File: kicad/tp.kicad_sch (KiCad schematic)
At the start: 16 parts, among them J2 MAX30102_Header, SW1 SWITCH_MODE, SW2 ALARM_OFF, U1 HM10

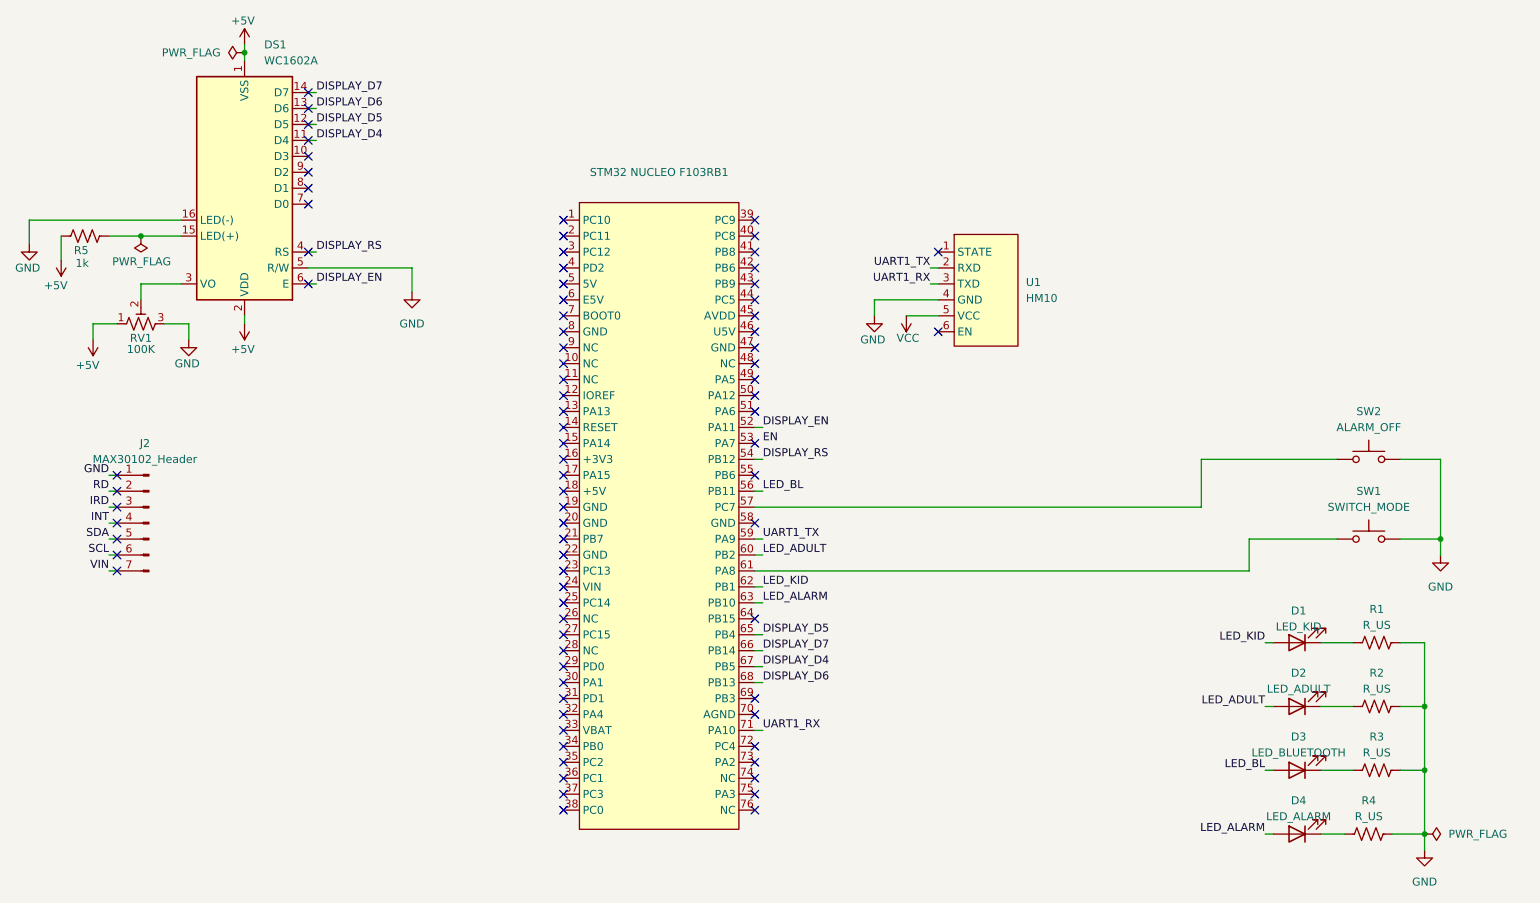
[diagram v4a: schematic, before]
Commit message: feat(sch): agrega symbols y conexiones faltantes
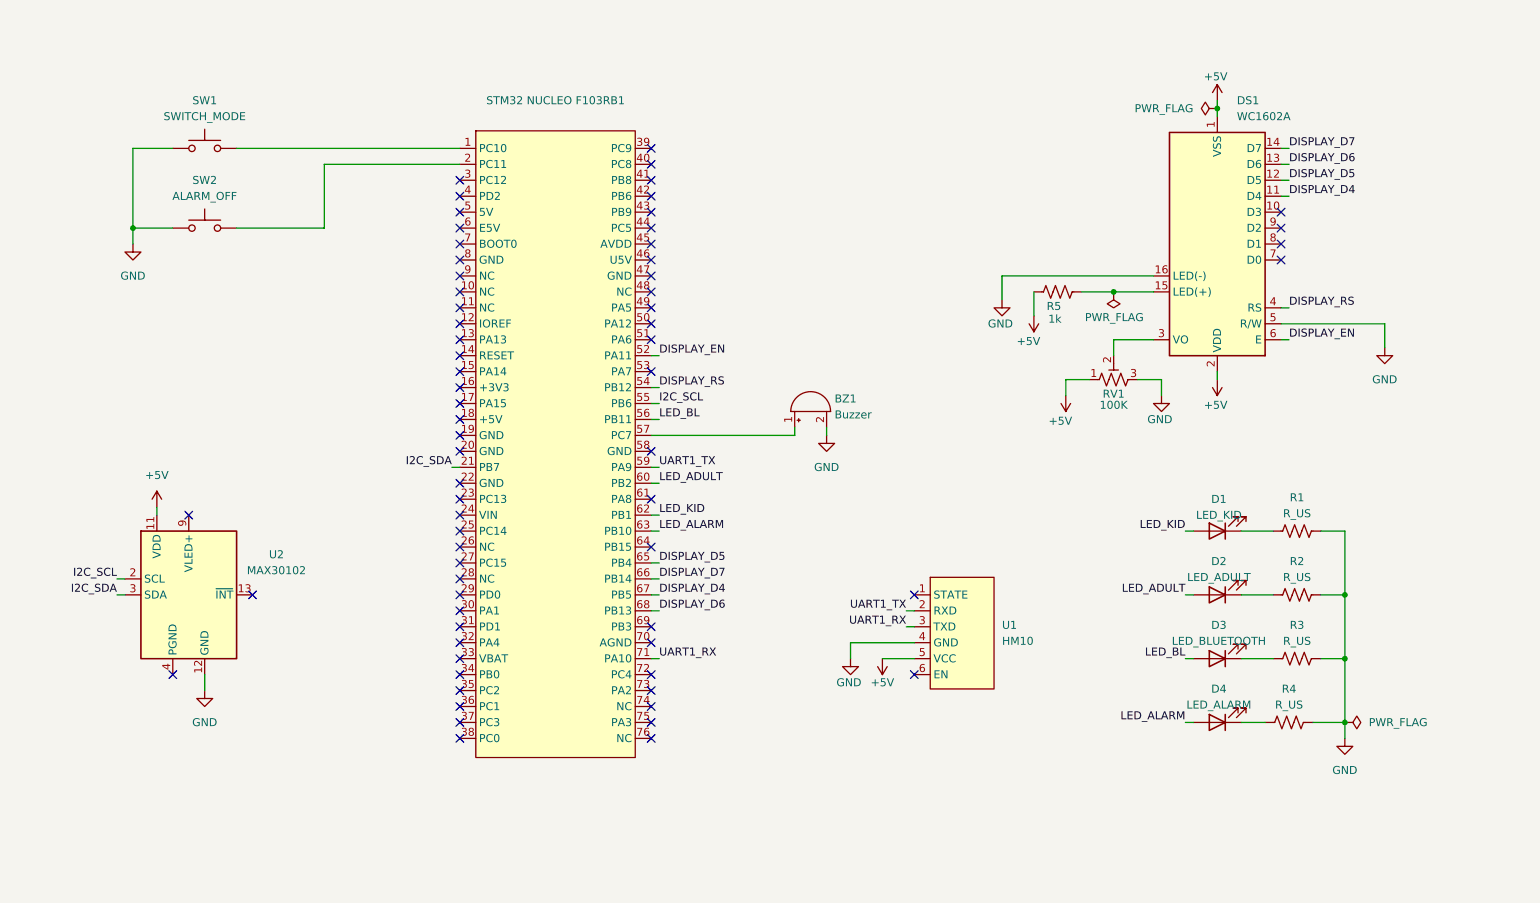
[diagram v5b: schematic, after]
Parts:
- removed J2: MAX30102_Header, symbol Connector:Conn_01x07_Pin
- added BZ1: Buzzer, symbol Device:Buzzer
- added U2: MAX30102, OptoDevice:Maxim_OLGA-14_3.3x5.6mm_P0.8mm, symbol Sensor:MAX30102
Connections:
- net VCC is gone; now on net +5V: U1.5 (VCC)
- net +5V: now also U2.11 (VDD)
- net GND: now also BZ1.2 (-), U2.12 (GND)
- net at SW1.2: now also STM32 NUCLEO F103RB1.1 (PC10); no longer STM32 NUCLEO F103RB1.61 (PA8)
- net at SW2.2: now also STM32 NUCLEO F103RB1.2 (PC11); no longer STM32 NUCLEO F103RB1.57 (PC7)
- net I2C_SDA: now reaches STM32 NUCLEO F103RB1.21 (PB7)
- net I2C_SDA: now also U2.3 (SDA)
- net I2C_SCL: now reaches STM32 NUCLEO F103RB1.55 (PB6)
- net I2C_SCL: now also U2.2 (SCL)
- new net: U2.10 (VLED+), U2.9 (VLED+)
- new net: BZ1.1 (+), STM32 NUCLEO F103RB1.57 (PC7)
- no-connect marks 81 -> 68
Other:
- moved on the sheet: D1, D2, D3, D4, DS1, R1, R2, R3, R4, R5, RV1, STM32 NUCLEO F103RB1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

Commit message: fix(sch): actualizo el simbolo de la nucleo
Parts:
- removed STM32 NUCLEO F103RB1: ~, symbol STM32_NUCLEO:NUCLEO-F103RB
- added U1: STM32 NUCLEO F103RB, STM32:NUCLEO F103RB, symbol STM32_NUCLEO:NUCLEO-F103RB
- renumbered U1 to U3
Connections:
- net DISPLAY_D4: now also U1.67 (PB5)
- net DISPLAY_D5: now also U1.65 (PB4)
- net DISPLAY_D6: now also U1.68 (PB13)
- net DISPLAY_D7: now also U1.66 (PB14)
- net DISPLAY_EN: now also U1.52 (PA11)
- net DISPLAY_RS: now also U1.54 (PB12)
- net I2C_SCL: now also U1.55 (PB6)
- net I2C_SDA: now also U1.21 (PB7)
- net LED_ADULT: now also U1.60 (PB2)
- net LED_ALARM: now also U1.63 (PB10)
- net LED_BL: now also U1.56 (PB11)
- net LED_KID: now also U1.62 (PB1)
- net UART1_RX: now also U1.71 (PA10)
- net UART1_TX: now also U1.59 (PA9)
- net at SW1.2: now also U1.1 (PC10)
- net at SW2.2: now also U1.2 (PC11)
- net at BZ1.1 (+): now also U1.57 (PC7)
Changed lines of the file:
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@@
 		(dnp no)
 		(fields_autoplaced yes)
-		(property "Reference" "U1"
+		(property "Reference" "U3"
 			(at 180.34 115.3159 0)
 			(effects
@@
 			(project ""
 				(path "/4321da81-5d44-4e9a-b537-a2876d1011a9"
-					(reference "U1")
+					(reference "U3")
 					(unit 1)
 				)
@@
 	)
 	(symbol
+		(lib_id "STM32_NUCLEO:NUCLEO-F103RB")
+		(at 109.22 85.09 0)
+		(unit 1)
+		(exclude_from_sim no)
+		(in_bom yes)
+		(on_board yes)
+		(dnp no)
+		(fields_autoplaced yes)
+		(property "Reference" "U1"
+			(at 109.22 31.75 0)
+			(effects
+				(font
+					(size 1.27 1.27)
+				)
+			)
+		)
+		(property "Value" "STM32 NUCLEO F103RB"
+			(at 109.22 34.29 0)
+			(effects
+				(font
+					(size 1.27 1.27)
+				)
+			)
+		)
+		(property "Footprint" "STM32:NUCLEO F103RB"
+			(at 109.22 85.09 0)
+			(effects
+				(font
+					(size 1.27 1.27)
+				)
+				(hide yes)
+			)
+		)
+		(property "Datasheet" ""
+			(at 109.22 85.09 0)
+			(effects
+				(font
+					(size 1.27 1.27)
+				)
+				(hide yes)
+			)
+		)
+		(property "Description" ""
+			(at 109.22 85.09 0)
+			(effects
+				(font
+					(size 1.27 1.27)
+				)
+				(hide yes)
+			)
+		)
+		(pin "66"
+		)
+		(pin "47"
+		)
+		(pin "43"
+		)
+		(pin "2"
+		)
+		(pin "44"
+		)
+		(pin "19"
+		)
+		(pin "63"
+		)
+		(pin "74"
+		)
+		(pin "73"
+		)
+		(pin "51"
+		)
+		(pin "67"
+		)
+		(pin "64"
+		)
+		(pin "55"
+		)
+		(pin "24"
+		)
+		(pin "37"
+		)
+		(pin "33"
+		)
+		(pin "50"
+		)
+		(pin "53"
+		)
+		(pin "27"
+		)
+		(pin "30"
+		)
+		(pin "34"
+		)
+		(pin "22"
+		)
+		(pin "57"
+		)
+		(pin "48"
+		)
+		(pin "56"
+		)
+		(pin "70"
+		)
+		(pin "60"
+		)
+		(pin "32"
+		)
+		(pin "42"
+		)
+		(pin "61"
+		)
+		(pin "28"
+		)
+		(pin "31"
+		)
+		(pin "58"
+		)
+		(pin "52"
+		)
+		(pin "62"
+		)
+		(pin "71"
+		)
+		(pin "46"
+		)
+		(pin "26"
+		)
+		(pin "45"
+		)
+		(pin "29"
+		)
+		(pin "65"
+		)
+		(pin "41"
+		)
+		(pin "38"
+		)
+		(pin "18"
+		)
+		(pin "54"
+		)
+		(pin "21"
+		)
+		(pin "20"
+		)
+		(pin "16"
+		)
+		(pin "9"
+		)
+		(pin "8"
+		)
+		(pin "7"
+		)
+		(pin "6"
+		)
+		(pin "5"
+		)
+		(pin "4"
+		)
+		(pin "3"
+		)
+		(pin "1"
+		)
+		(pin "15"
+		)
+		(pin "14"
+		)
+		(pin "13"
+		)
+		(pin "12"
+		)
+		(pin "11"
+		)
+		(pin "10"
+		)
+		(pin "23"
+		)
+		(pin "72"
+		)
+		(pin "68"
+		)
+		(pin "75"
+		)
+		(pin "76"
+		)
+		(pin "17"
+		)
+		(pin "25"
+		)
+		(pin "59"
+		)
+		(pin "39"
+		)
+		(pin "69"
+		)
+		(pin "40"
+		)
+		(pin "36"
+		)
+		(pin "35"
+		)
+		(pin "49"
+		)
+		(instances
+			(project ""
+				(path "/4321da81-5d44-4e9a-b537-a2876d1011a9"
+					(reference "U1")
+					(unit 1)
+				)
+			)
+		)
+	)
+	(symbol
 		(lib_id "power:PWR_FLAG")
 		(at 234.95 130.81 270)
@@
 					(unit 1)
 				)
-			)
-		)
-	)
-	(symbol
-		(lib_id "STM32_NUCLEO:NUCLEO-F103RB")
-		(at 109.22 85.09 0)
-		(unit 1)
-		(exclude_from_sim no)
-		(in_bom yes)
-		(on_board yes)
-		(dnp no)
-		(fields_autoplaced yes)
-		(property "Reference" "STM32 NUCLEO F103RB1"
-			(at 109.22 31.75 0)
-			(effects
-				(font
-					(size 1.27 1.27)
-				)
-			)
-		)
-		(property "Value" "~"
-			(at 109.22 34.29 0)
-			(effects
-				(font
-					(size 1.27 1.27)
-				)
-			)
-		)
-		(property "Footprint" ""
-			(at 109.22 85.09 0)
-			(effects
-				(font
-					(size 1.27 1.27)
-				)
-				(hide yes)
-			)
-		)
-		(property "Datasheet" ""
-			(at 109.22 85.09 0)
-			(effects
-				(font
-					(size 1.27 1.27)
-				)
-				(hide yes)
-			)
-		)
-		(property "Description" ""
-			(at 109.22 85.09 0)
-			(effects
-				(font
-					(size 1.27 1.27)
-				)
-				(hide yes)
-			)
-		)
-		(pin "21"
-		)
-		(pin "75"
-		)
-		(pin "20"
-		)
-		(pin "63"
-		)
-		(pin "60"
-		)
-		(pin "61"
-		)
-		(pin "59"
-		)
-		(pin "58"
-		)
-		(pin "57"
-		)
-		(pin "70"
-		)
-		(pin "74"
-		)
-		(pin "72"
-		)
-		(pin "73"
-		)
-		(pin "71"
-		)
-		(pin "76"
-		)
-		(pin "2"
-		)
-		(pin "56"
-		)
-		(pin "23"
-		)
-		(pin "42"
-		)
-		(pin "44"
-		)
-		(pin "43"
-		)
-		(pin "32"
-		)
-		(pin "26"
-		)
-		(pin "50"
-		)
-		(pin "51"
-		)
-		(pin "52"
-		)
-		(pin "54"
-		)
-		(pin "53"
-		)
-		(pin "48"
-		)
-		(pin "49"
-		)
-		(pin "45"
-		)
-		(pin "35"
-		)
-		(pin "39"
-		)
-		(pin "33"
-		)
-		(pin "27"
-		)
-		(pin "28"
-		)
-		(pin "19"
-		)
-		(pin "25"
-		)
-		(pin "24"
-		)
-		(pin "65"
-		)
-		(pin "64"
-		)
-		(pin "29"
-		)
-		(pin "30"
-		)
-		(pin "22"
-		)
-		(pin "46"
-		)
-		(pin "47"
-		)
-		(pin "40"
-		)
-		(pin "41"
-		)
-		(pin "34"
-		)
-		(pin "62"
-		)
-		(pin "66"
-		)
-		(pin "31"
-		)
-		(pin "18"
-		)
-		(pin "69"
-		)
-		(pin "67"
-		)
-		(pin "68"
-		)
-		(pin "55"
-		)
-		(pin "36"
-		)
-		(pin "37"
-		)
-		(pin "17"
-		)
-		(pin "8"
-		)
-		(pin "7"
-		)
-		(pin "6"
-		)
-		(pin "5"
-		)
-		(pin "4"
-		)
-		(pin "3"
-		)
-		(pin "1"
-		)
-		(pin "38"
-		)
-		(pin "16"
-		)
-		(pin "15"
-		)
-		(pin "14"
-		)
-		(pin "13"
-		)
-		(pin "12"
-		)
-		(pin "11"
-		)
-		(pin "10"
-		)
-		(pin "9"
-		)
-		(instances
-			(project ""
-				(path "/4321da81-5d44-4e9a-b537-a2876d1011a9"
-					(reference "STM32 NUCLEO F103RB1")
-					(unit 1)
-				)

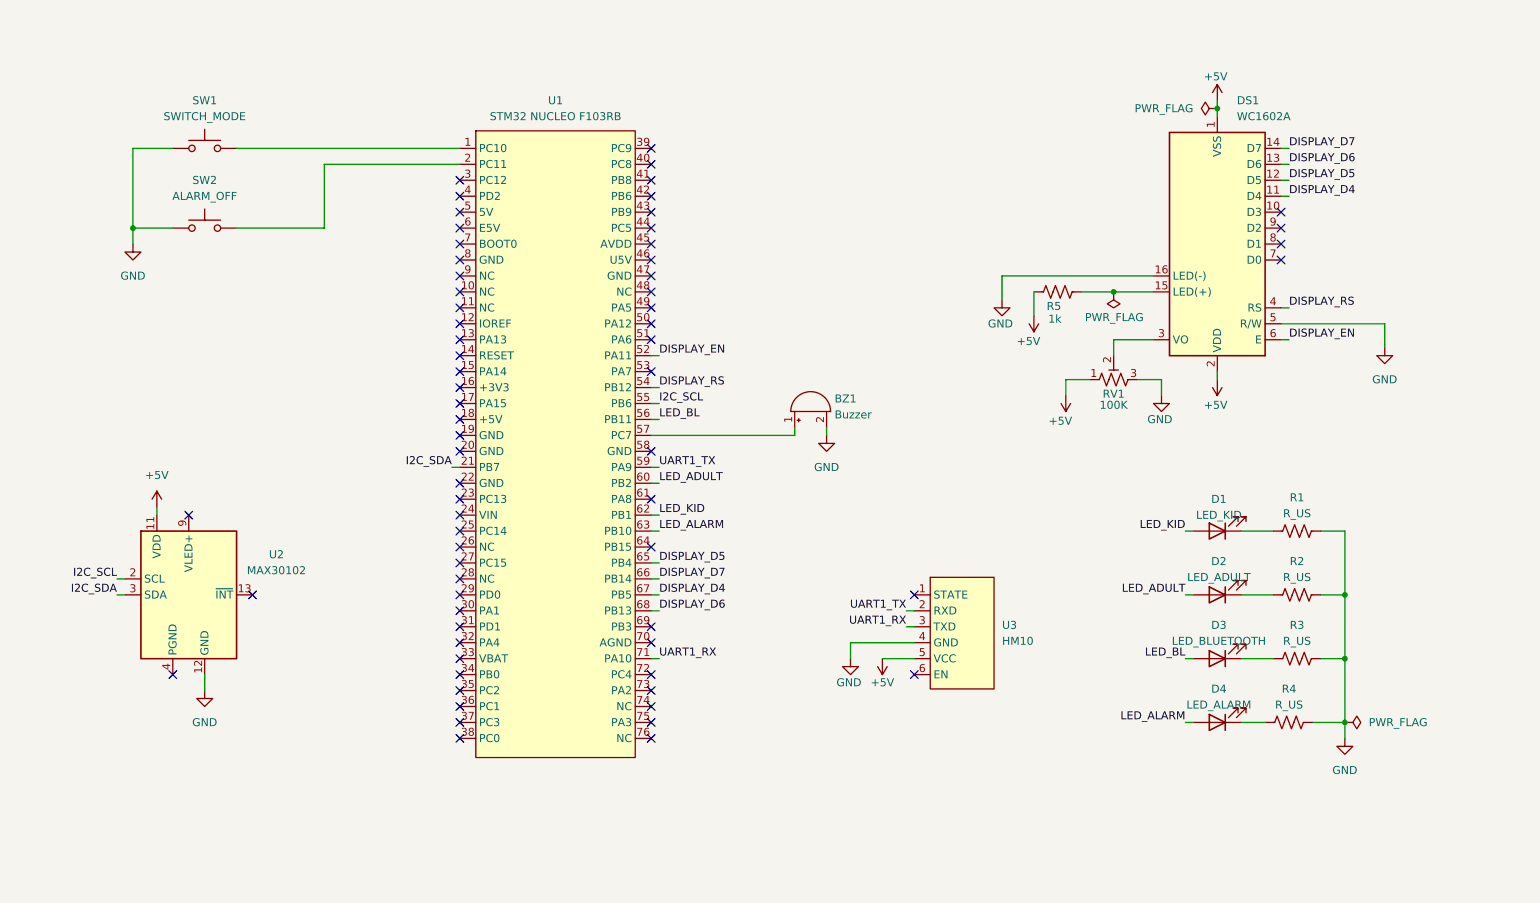
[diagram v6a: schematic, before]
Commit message: feat(sch): agrego las footprints de los componentes
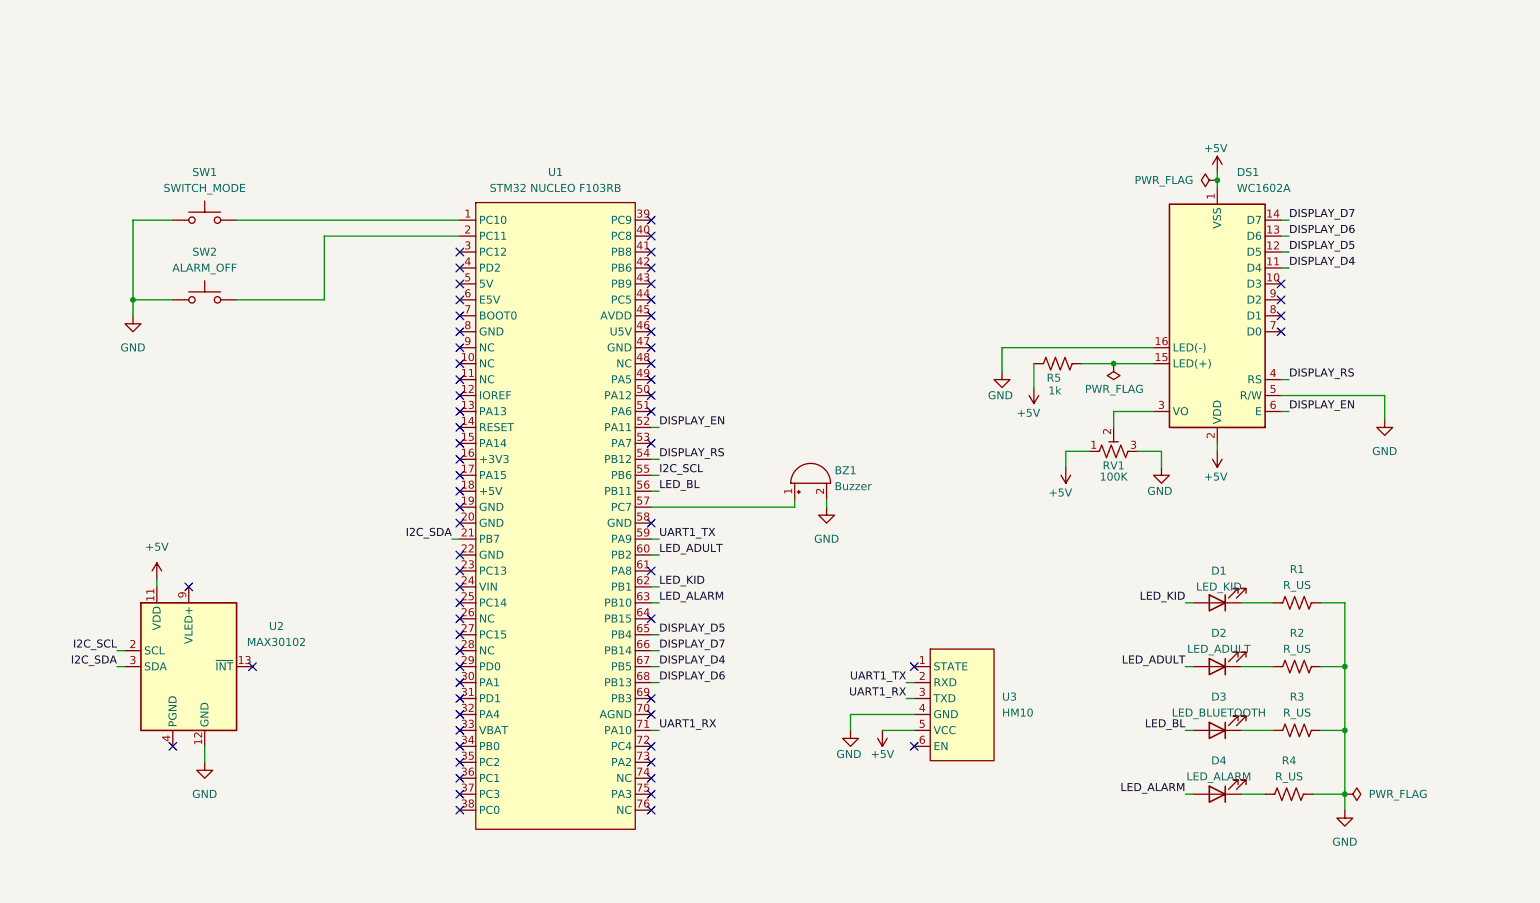
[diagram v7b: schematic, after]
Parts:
- BZ1: footprint (none) -> Buzzer_Beeper:Buzzer_12x9.5RM7.6
- D1, D2, D3, D4: footprint (none) -> LED_THT:LED_D5.0mm
- R1, R2, R3, R4, R5: footprint (none) -> Resistor_THT:R_Axial_DIN0207_L6.3mm_D2.5mm_P7.62mm_Horizontal
- RV1: footprint (none) -> Potentiometer_THT:Potentiometer_Alps_RK163_Single_Horizontal
- SW1, SW2: footprint (none) -> Button_Switch_THT:SW_PUSH-12mm_Wuerth-430476085716
- U3: footprint (none) -> Connector_PinSocket_2.54mm:PinSocket_1x06_P2.54mm_Vertical
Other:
- moved on the sheet: BZ1, D1, D2, D3, D4, DS1, R1, R2, R3, R4, R5, RV1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

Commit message: feat(sch): agrega symbol custom del max30102
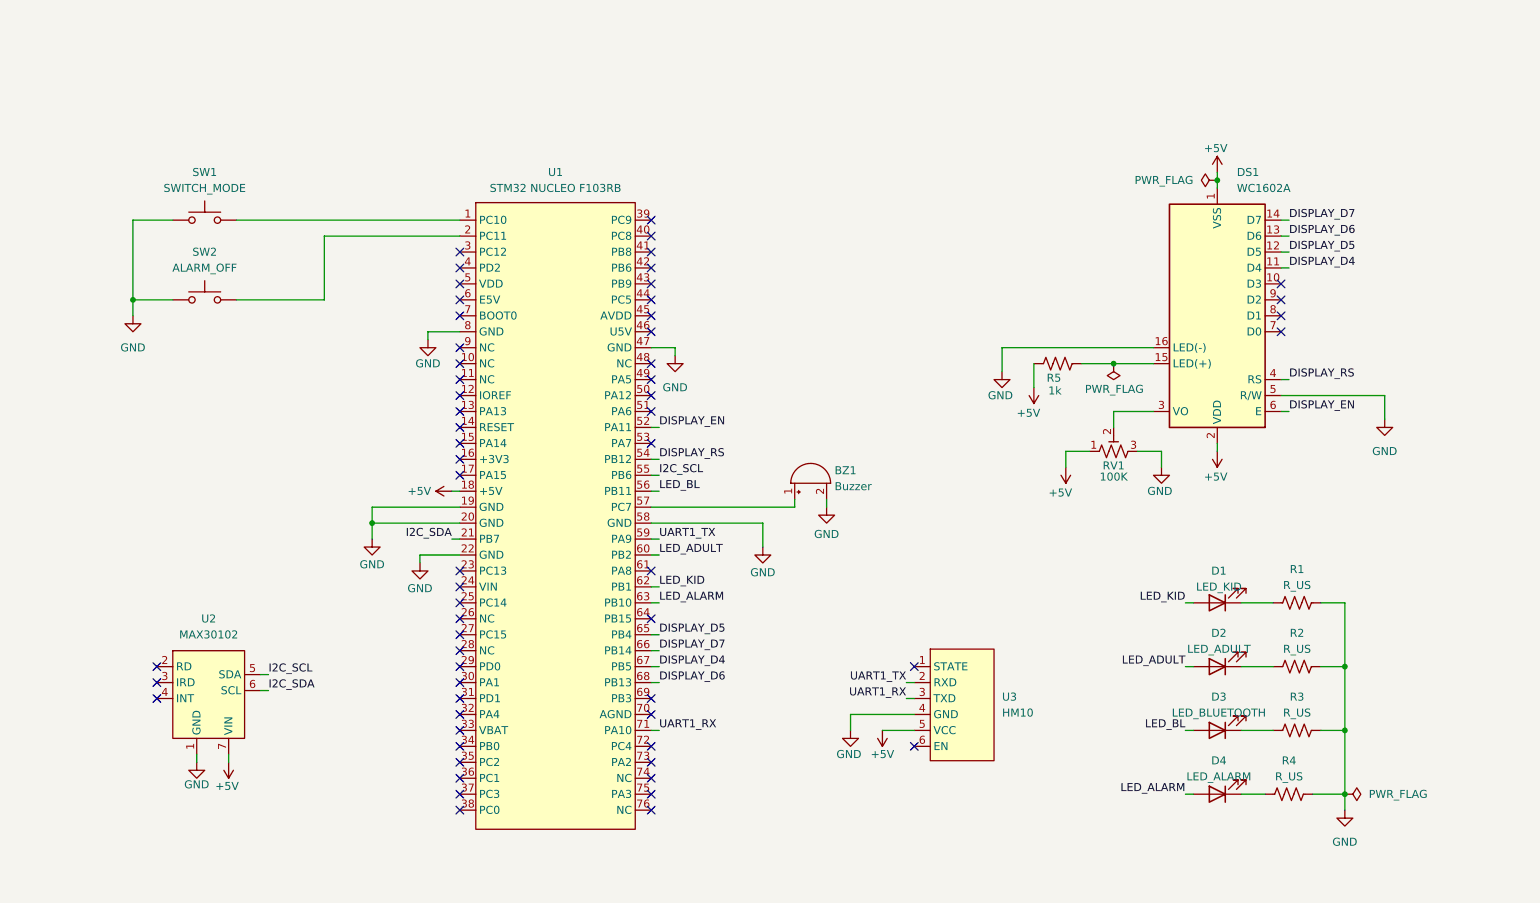
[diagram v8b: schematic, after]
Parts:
- U2: footprint OptoDevice:Maxim_OLGA-14_3.3x5.6mm_P0.8mm -> Connector_PinHeader_2.54mm:PinHeader_1x06_P2.54mm_Vertical; symbol Sensor:MAX30102 -> STM32_NUCLEO:MAX30102-Header
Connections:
- net +5V: now also U1.18 (+5V), U2.7 (VIN); no longer U2.11 (VDD)
- net GND: now also U1.19 (GND), U1.20 (GND), U1.22 (GND), U1.47 (GND), U1.58 (GND), U1.8 (GND), U2.1 (GND); no longer U2.12 (GND)
- net I2C_SCL: now also U2.5 (SDA); no longer U2.2 (SCL)
- net I2C_SDA: now also U2.6 (SCL); no longer U2.3 (SDA)
- no-connect marks 68 -> 61
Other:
- moved on the sheet: U2
